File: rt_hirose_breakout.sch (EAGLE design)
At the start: 2 parts

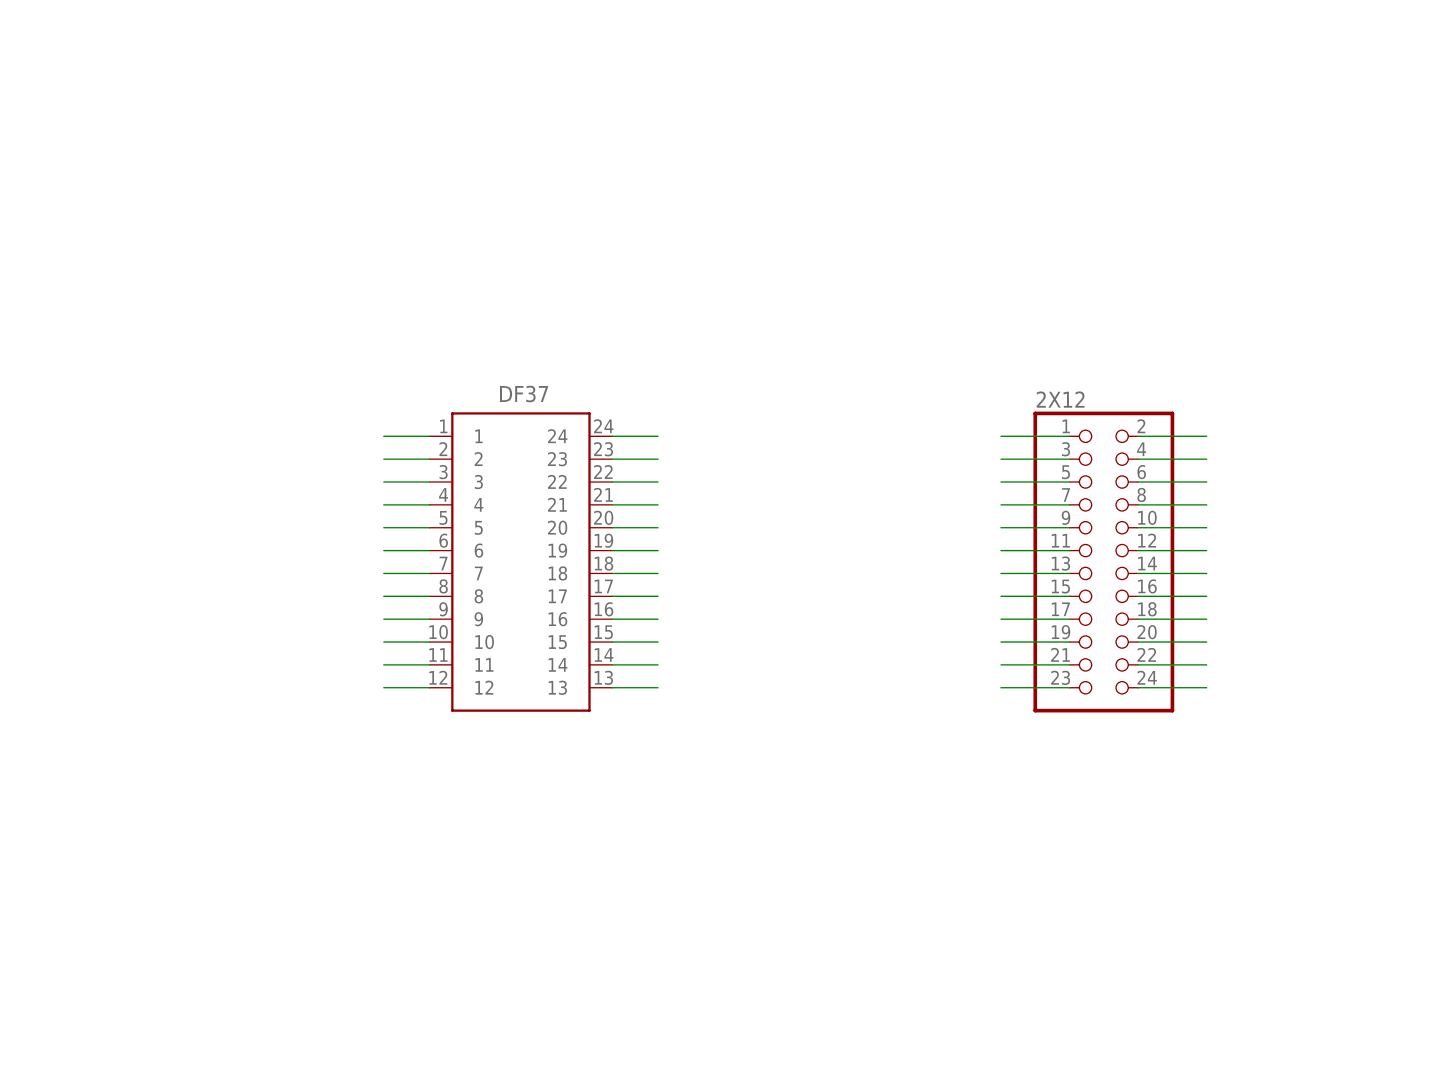
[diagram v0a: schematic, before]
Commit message: add SWD connector, though the VCC might *not* be (even equivalent to) the STM32 VDD, which would be a major problem
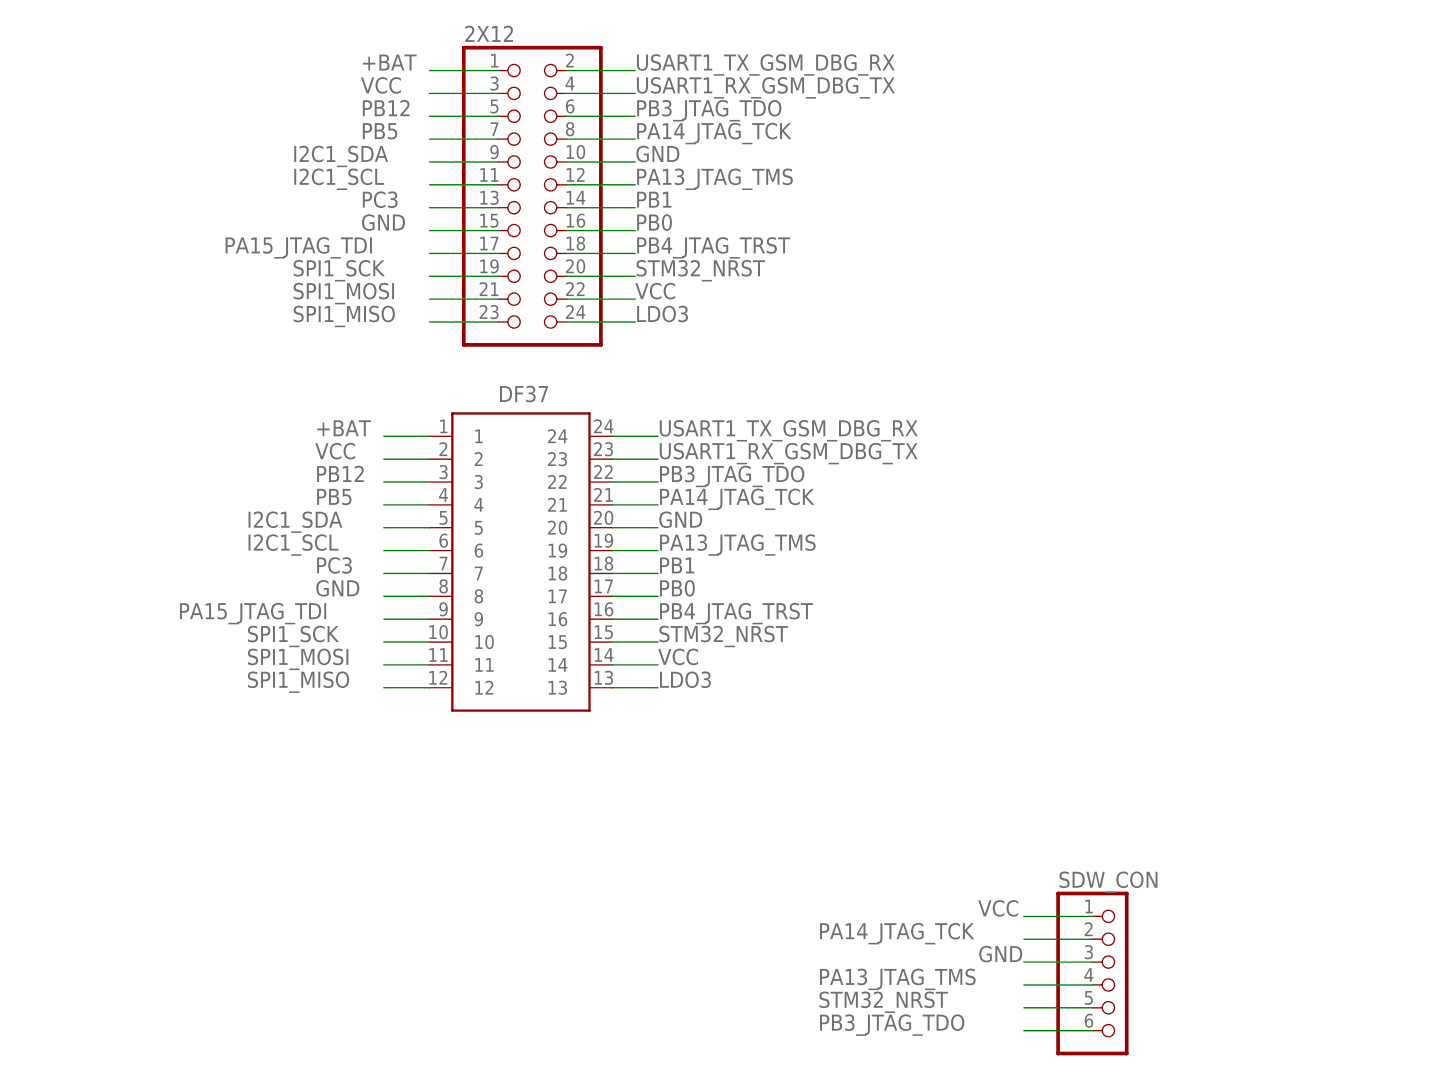
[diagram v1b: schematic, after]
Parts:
- added SDW_CON: (no value), pinhead:PINHD-1X6
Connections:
- removed net PA14_JTAF_TCK: 2X12.8, DF37.21
- new net PA14_JTAG_TCK: 2X12.8, DF37.21, SDW_CON.2
- net GND: now also SDW_CON.3
- net PA13_JTAG_TMS: now also SDW_CON.4
- net PB3_JTAG_TDO: now also SDW_CON.6
- net STM32_NRST: now also SDW_CON.5
- net VCC: now also SDW_CON.1
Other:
- moved on the sheet: 2X12

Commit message: The VCCs might not be the same, at least not in the future...
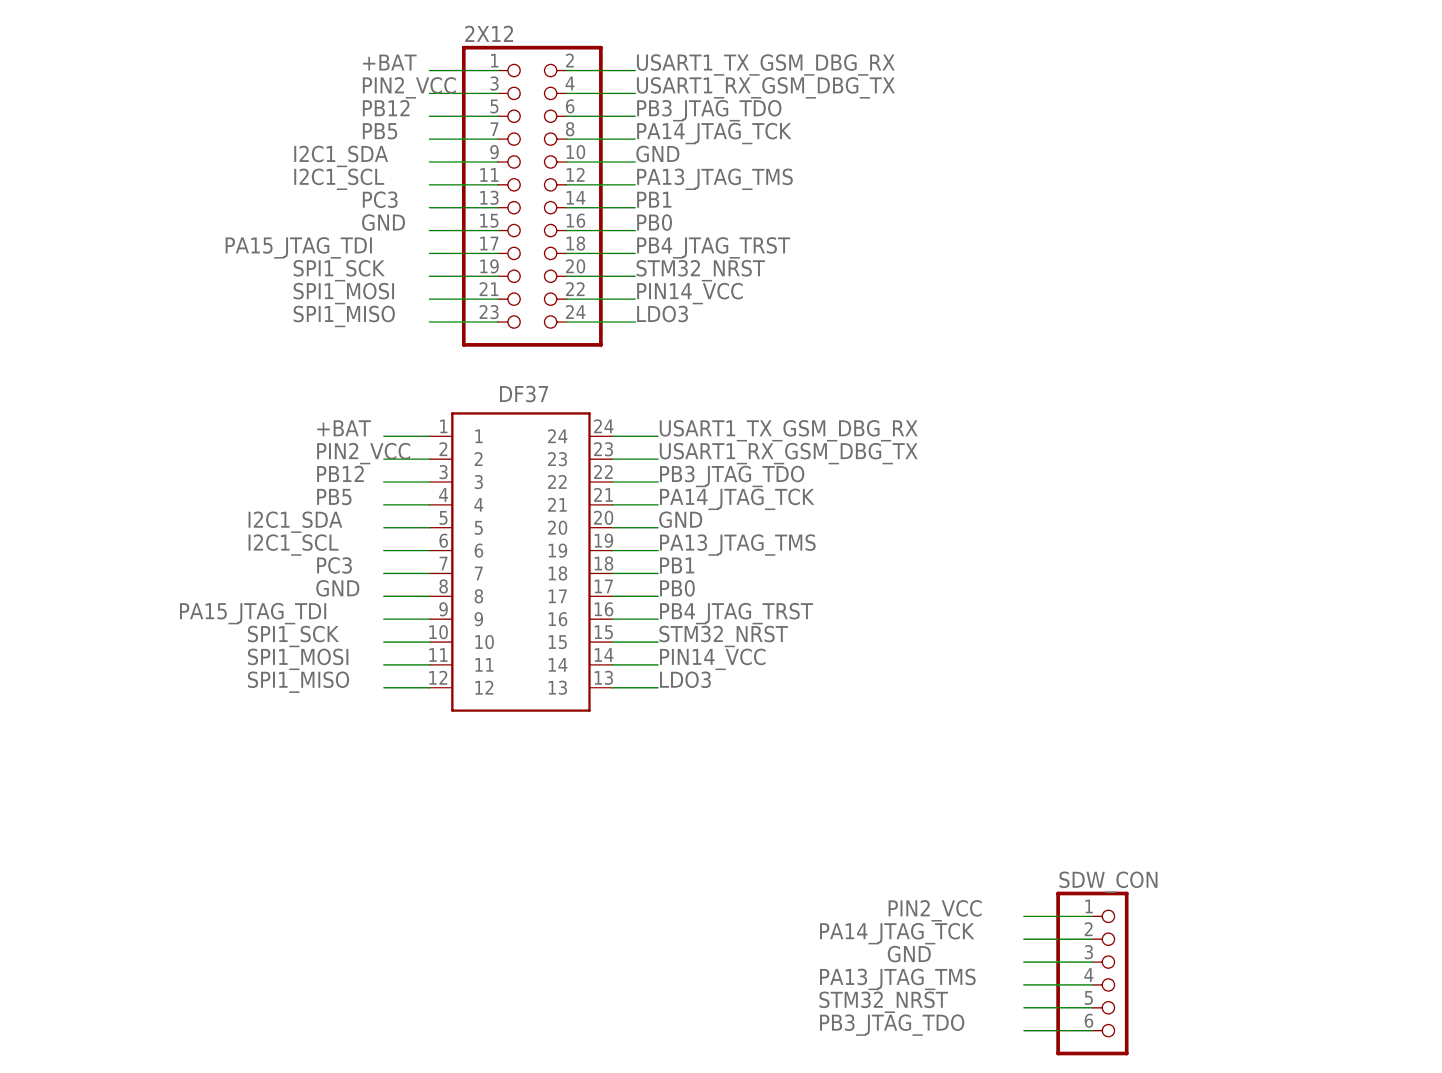
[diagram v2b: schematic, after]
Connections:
- removed net VCC: 2X12.22, 2X12.3, DF37.14, DF37.2, SDW_CON.1
- new net PIN14_VCC: 2X12.22, DF37.14
- new net PIN2_VCC: 2X12.3, DF37.2, SDW_CON.1

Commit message: use solder jumpers to select which "vcc" pin to use for SWD VDD
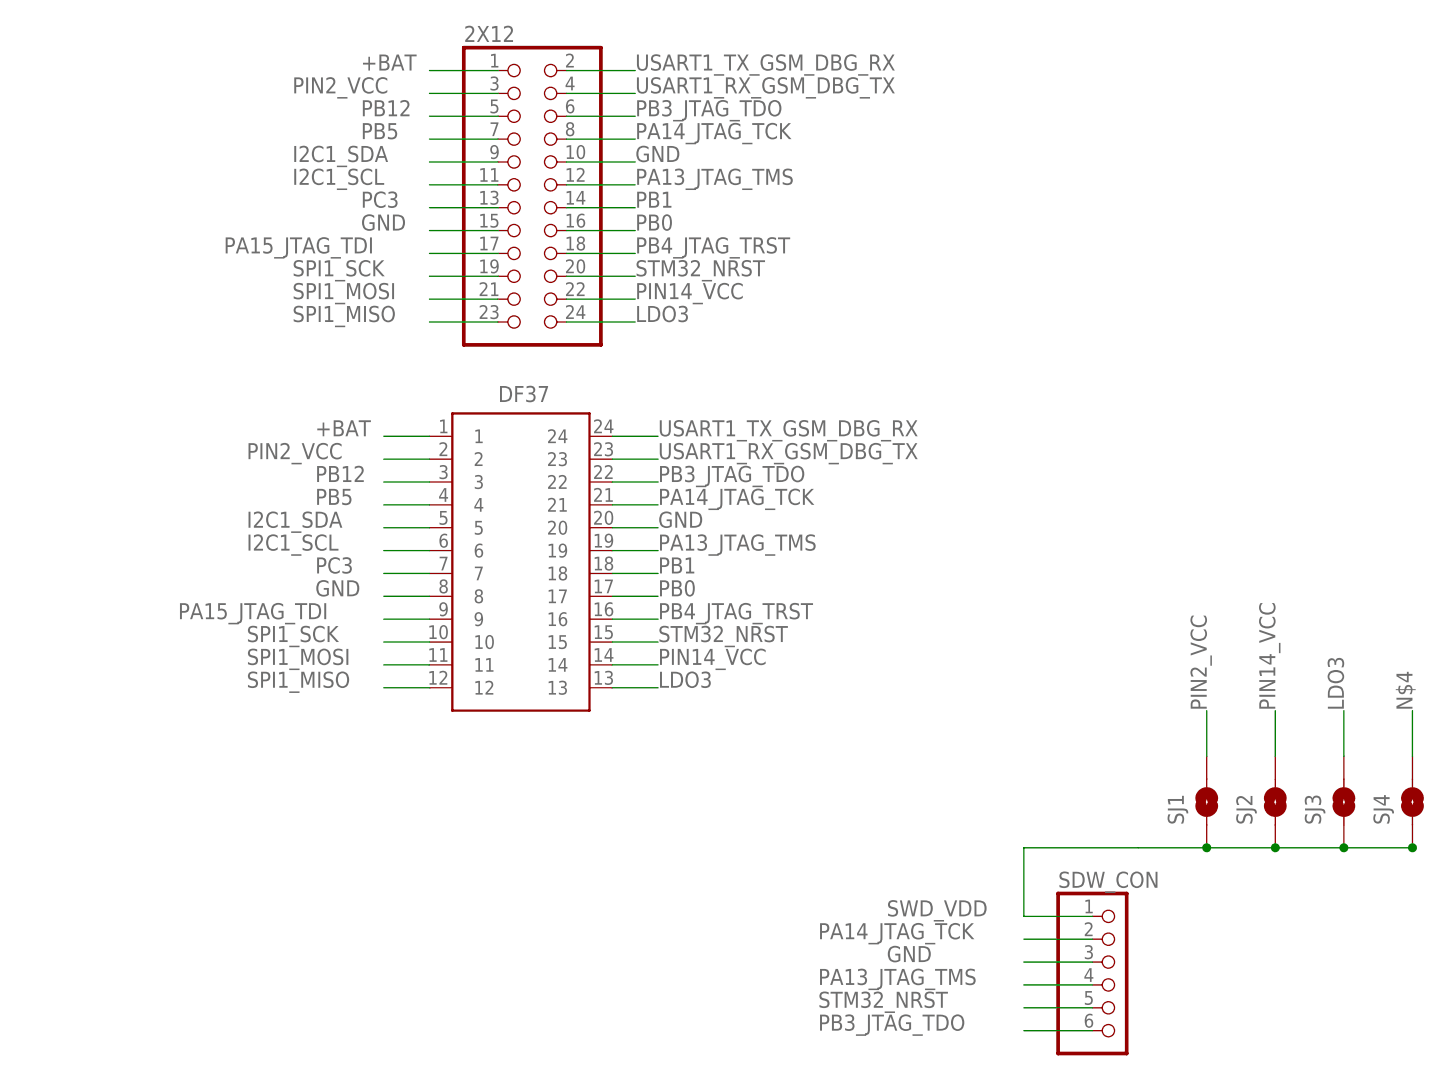
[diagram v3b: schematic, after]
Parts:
- added SJ1, SJ2, SJ3, SJ4: SOLDERJUMPERNO, SparkFun-Passives:SOLDERJUMPERNO
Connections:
- new net N$4: SJ4.2
- new net SWD_VDD: SDW_CON.1, SJ1.1, SJ2.1, SJ3.1, SJ4.1
- net LDO3: now also SJ3.2
- net PIN14_VCC: now also SJ2.2
- net PIN2_VCC: now also SJ1.2; no longer SDW_CON.1

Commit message: add reset switch
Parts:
- added RESET: (no value), SparkFun-Electromechanical:TAC_SWITCHSMD
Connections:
- net GND: now also RESET.3, RESET.4
- net STM32_NRST: now also RESET.1, RESET.2
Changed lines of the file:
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@@
 <part name="SJ3" library="SparkFun-Passives" deviceset="SOLDERJUMPER" device="NO"/>
 <part name="SJ4" library="SparkFun-Passives" deviceset="SOLDERJUMPER" device="NO"/>
+<part name="RESET" library="SparkFun-Electromechanical" deviceset="TAC_SWITCH" device="SMD"/>
 </parts>
 <sheets>
@@
 <attribute name="NAME" x="139.7" y="27.94" size="1.778" layer="95" rot="R90"/>
 </instance>
+<instance part="RESET" gate="S" x="10.16" y="7.62"/>
 </instances>
 <busses>
@@
 <label x="83.82" y="12.7" size="1.778" layer="95"/>
 </segment>
+<segment>
+<pinref part="RESET" gate="S" pin="4"/>
+<pinref part="RESET" gate="S" pin="3"/>
+<wire x1="15.24" y1="5.08" x2="15.24" y2="7.62" width="0.1524" layer="91"/>
+<wire x1="15.24" y1="7.62" x2="17.78" y2="7.62" width="0.1524" layer="91"/>
+<junction x="15.24" y="7.62"/>
+<label x="17.78" y="7.62" size="1.778" layer="95"/>
+</segment>
 </net>
 <net name="PA15_JTAG_TDI" class="0">
@@
 <label x="76.2" y="7.62" size="1.778" layer="95"/>
 </segment>
-</net>
+<segment>
+<pinref part="RESET" gate="S" pin="1"/>
+<wire x1="5.08" y1="7.62" x2="2.54" y2="7.62" width="0.1524" layer="91"/>
+<pinref part="RESET" gate="S" pin="2"/>
+<wire x1="5.08" y1="7.62" x2="5.08" y2="5.08" width="0.1524" layer="91"/>
+<junction x="5.08" y="7.62"/>
+<label x="-12.7" y="7.62" size="1.778" layer="95"/>
+</segment>
+</net>
